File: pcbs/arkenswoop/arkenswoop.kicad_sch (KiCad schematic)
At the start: 60 parts, among them J1 TRRS, SW1 Choc, SW10 Choc, SW11 Choc, SW12 Choc, SW13 Choc, SW14 Choc, SW15 Choc, SW16 Choc, SW17 Choc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

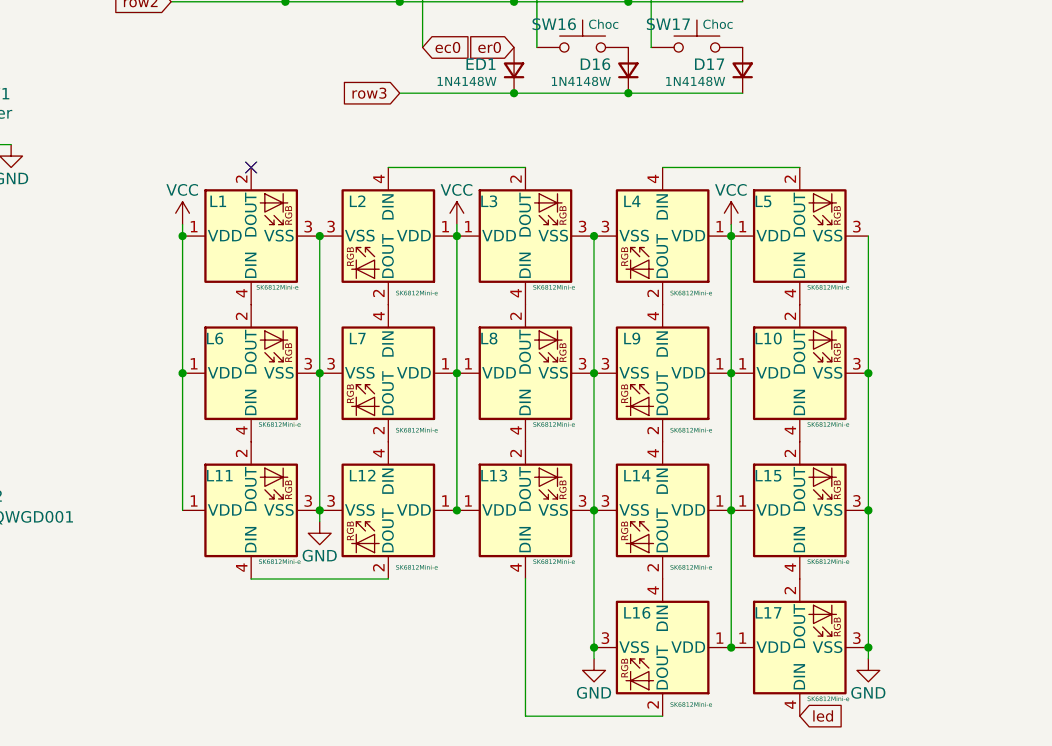
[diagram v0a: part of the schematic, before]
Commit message: removed leds from schematic
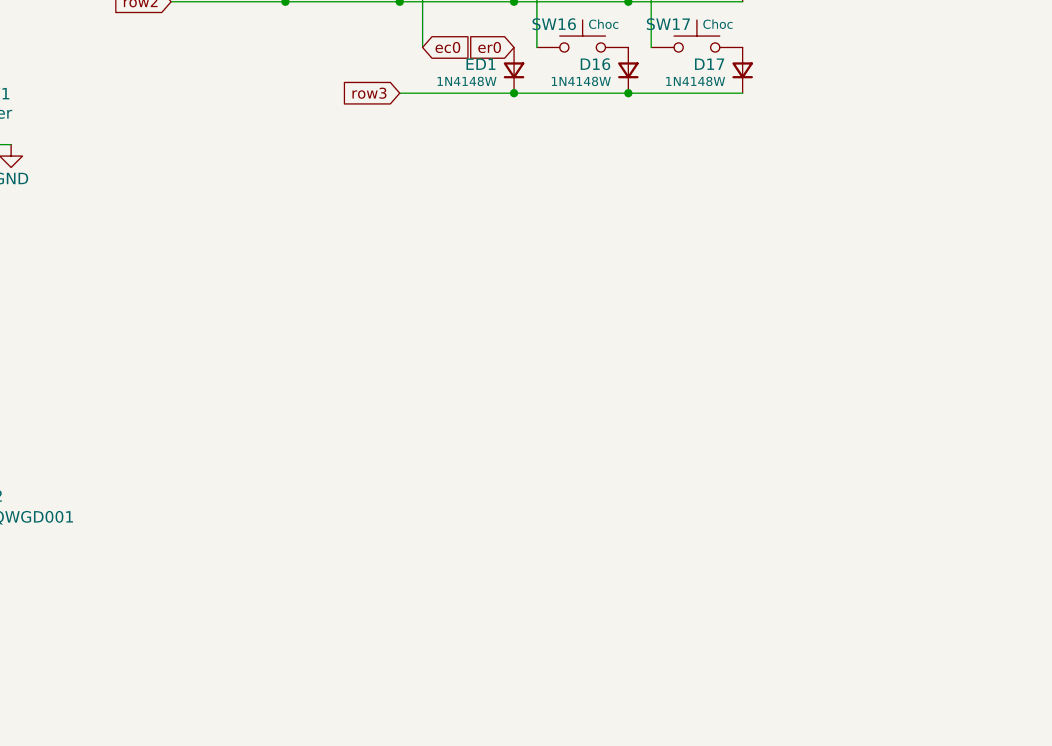
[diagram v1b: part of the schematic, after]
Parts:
- removed L1, L10, L11, L12, L13, L14, L15, L16, L17, L2, L3, L4, L5, L6, L7, L8, L9: SK6812Mini-e, swoop:SK6812_Mini_E, symbol swoop:SK6812MINI-E
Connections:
- no-connect marks 6 -> 5
